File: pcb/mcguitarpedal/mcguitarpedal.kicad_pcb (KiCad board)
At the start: 2 copper layers, 123 x 118 mm, 98 parts, among them J1 IN, J10 ENCODER2, J11 ENCODER3, J2 PREAMP_HEADERS, J3 BTN_MTX, J4 OUT, J5 EXP, J6 ILI9488 Module, J7 PWR_IN, J8 POT_HP_VOLUME_10k, J9 ENCODER1, Q1 Q_NPN_BCE, Q2 Q_PNP_BCE, SW1 SW_BYPASS, SW2 SW_TUNER, SW3 SW_PRESET, SW4 LINE_LEVEL, SW5 SW_PWR, U1 Teensy4.1, U2 Teensy Audio Board, U3 LM4562, U4 74HC148, U6 STPDWN-3P-5V, U7 STDN-3A24-ADJ, U8 74HCT595D

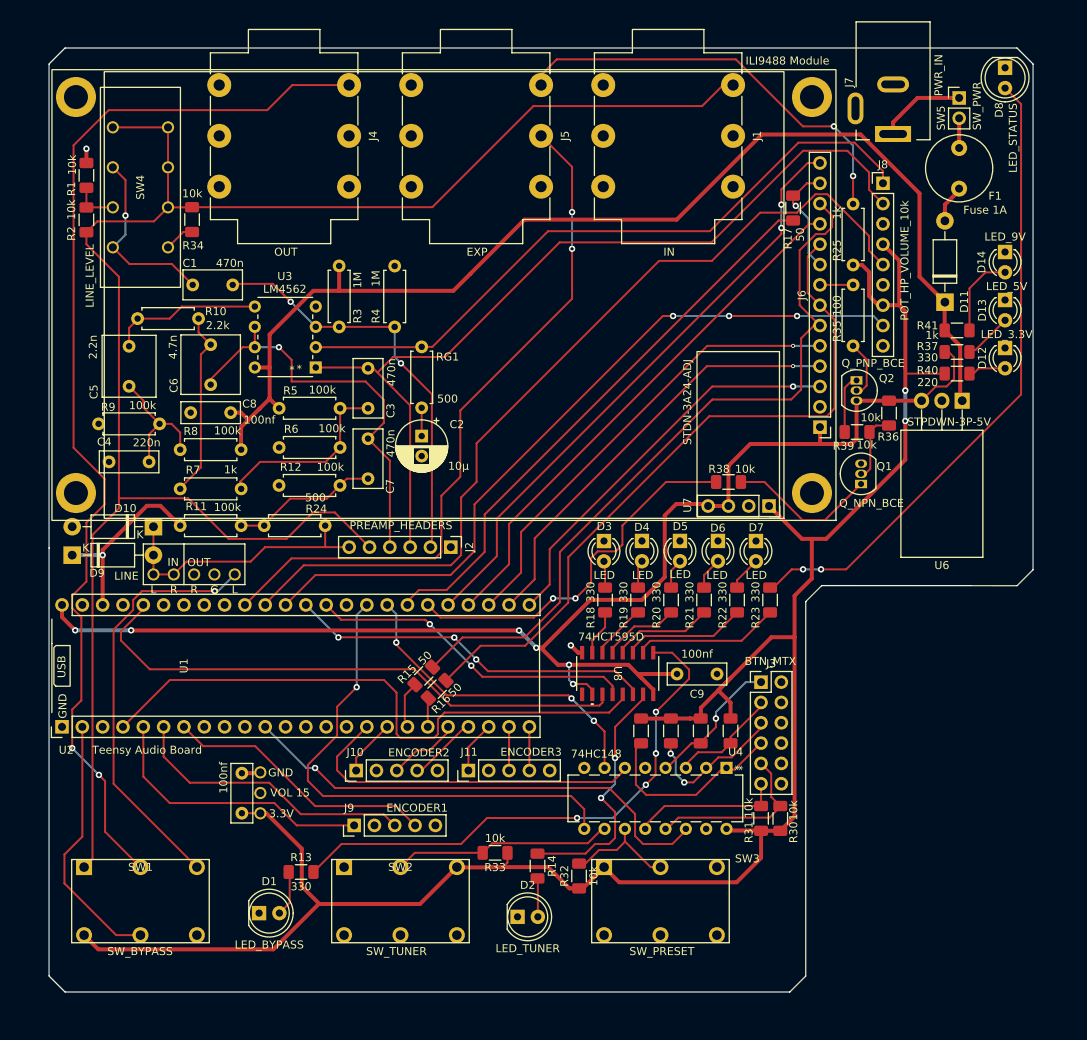
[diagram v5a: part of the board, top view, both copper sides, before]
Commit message: Rearranged pullups
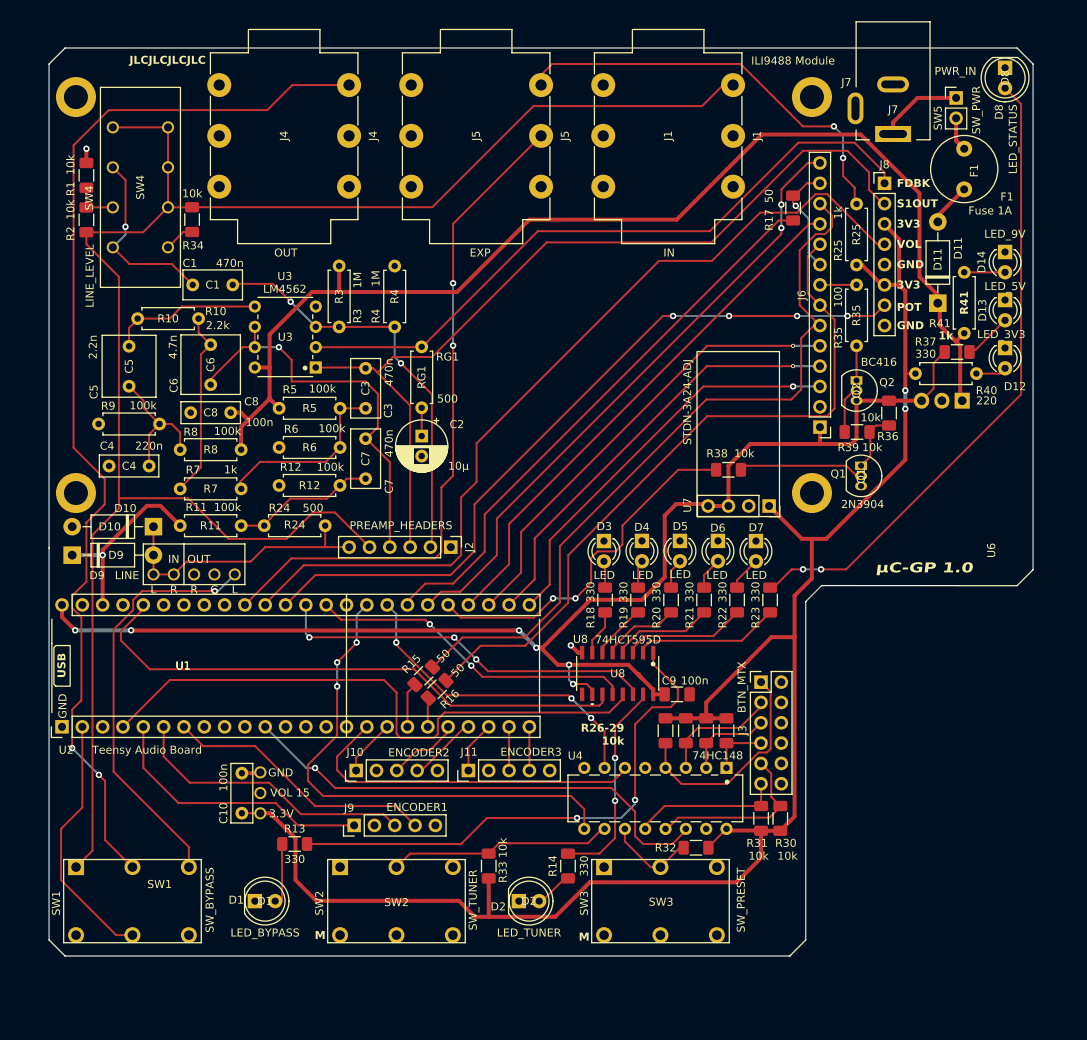
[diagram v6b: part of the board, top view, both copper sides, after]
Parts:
- C10, C8: value 100nf -> 100n
- C9: value 100nf -> 100n; footprint Capacitor_THT:C_Rect_L7.2mm_W2.5mm_P5.00mm_FKS2_FKP2_MKS2_MKP2 -> Capacitor_SMD:C_1206_3216Metric_Pad1.33x1.80mm_HandSolder
- D12: value LED_3.3V -> LED_3V3
- J8: footprint Connector_PinHeader_2.54mm:PinHeader_1x09_P2.54mm_Vertical -> mcguitarpedal:POTS_HEADER
- Q1: value Q_NPN_BCE -> 2N3904
- Q2: value Q_PNP_BCE -> BC416
- R40, R41: footprint Resistor_SMD:R_1206_3216Metric_Pad1.30x1.75mm_HandSolder -> Resistor_THT:R_Axial_DIN0207_L6.3mm_D2.5mm_P7.62mm_Horizontal
- U1: footprint mcguitarpedal:Teensy 4.1 -> mcguitarpedal:Teensy 4.1 with audio board
- U6: footprint Package_TO_SOT_THT:TO-220-3_Horizontal_TabDown -> mcguitarpedal:STPDWN-3P-5V
- moved R32 15.0 mm to (134.4, 125.0), turned to 180 degrees
- moved R26 10.7 mm to (138.2, 110.3)
- moved R41 7.31 mm to (167.9, 53.0), turned to -90 degrees
- moved C9 5.60 mm to (132.0, 105.8)
- moved R28 5.59 mm to (133.1, 110.3)
- moved R27 4.41 mm to (135.6, 110.3)
- moved R29 4.40 mm to (130.6, 110.3)
- moved R14 3.81 mm to (118.4, 127.3)
- moved R13 3.59 mm to (84.2, 124.5)
- moved R40 2.42 mm to (169.4, 65.7)
- moved Q1 2.28 mm to (155.0, 77.2), turned to -90 degrees
- moved D2 1.97 mm to (112.2, 131.6)
- moved R33 1.83 mm to (108.5, 127.3), turned to 90 degrees
- moved D1 1.59 mm to (79.2, 131.6)
- moved R38 1.53 mm to (138.4, 77.7)
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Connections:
- net /LED_STR renamed /22_LED_SHIFT_CLK
- net /SCK renamed /13_LED_STORE_CLK
- J6 pad 14: /37_TFT_T_IRQ -> /38_TFT_T_IRQ
- Q1 pad 1: Net-(Q1-B) -> Net-(Q1-C)
- Q1 pad 2: Net-(Q1-C) -> Net-(Q1-B)
- Q2 pad 1: Net-(Q2-B) -> Net-(Q2-C)
- Q2 pad 2: Net-(Q2-C) -> Net-(Q2-B)
- R38 pad 1: /38_BACKLIGHT_PWM -> /37_BACKLIGHT_PWM
- SW1 pad 4: 3.3V -> GND
- SW1 pad 6: GND -> unconnected-(SW1-C-Pad6)
- SW2 pad 3: 3.3V -> unconnected-(SW2-C-Pad3)
- SW3 pad 1: 3.3V -> GND
- SW3 pad 3: GND -> unconnected-(SW3-C-Pad3)
- U1 pad 29: /37_TFT_T_IRQ -> /37_BACKLIGHT_PWM
- U1 pad 30: /38_BACKLIGHT_PWM -> /38_TFT_T_IRQ
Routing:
- net /38_TFT_T_IRQ: track 0.00 -> 77.9 mm, vias 0 -> 2
- net /37_TFT_T_IRQ: track 75.4 -> 0.00 mm, vias 2 -> 0
- net /38_BACKLIGHT_PWM: track 46.9 -> 0.00 mm, vias 2 -> 0
- net /37_BACKLIGHT_PWM: track 0.00 -> 45.0 mm, vias 0 -> 2
- net 3.3V: track 260.1 -> 217.9 mm
- net Net-(J3-Pin_7): track 24.3 -> 7.42 mm
- net Net-(J3-Pin_1): track 17.3 -> 27.7 mm, vias 1 -> 0
- net Net-(J3-Pin_5): track 18.0 -> 11.0 mm, vias 2 -> 0
- net Net-(D14-A): track 10.5 -> 5.11 mm
- net Net-(U8-Q0): track 30.8 -> 25.6 mm
- net 5V: track 172.3 -> 167.4 mm
- net /A3_EXP: track 87.7 -> 84.5 mm
- net Net-(Q1-B): track 18.9 -> 15.8 mm
- net /SW3: track 14.1 -> 11.0 mm
- net Net-(Q2-C): track 7.20 -> 4.32 mm
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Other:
- board size 123 x 118 mm -> 123 x 113.5 mm
- board text added: "JLCJLCJLCJLC"
- board text added: "M"
- board text added: "R26-29 10k"
- board text added: "TODO: Testpoints Mounting holes Header silkscreen labels Silkscreen in general Decoupling caps for U4-7 (SMD ceramic?) Double check 8-to-3 pinout"
- board text added: "µC-GP 1.0"
- board text removed: "TODO: Backlight brightness PWR and status LEDs Testpoints Mounting holes Header silkscreen labels Silkscreen in general Decrease board size (Move inputs down?) Decoupling caps for U4-7 (SMD ceramic?)"

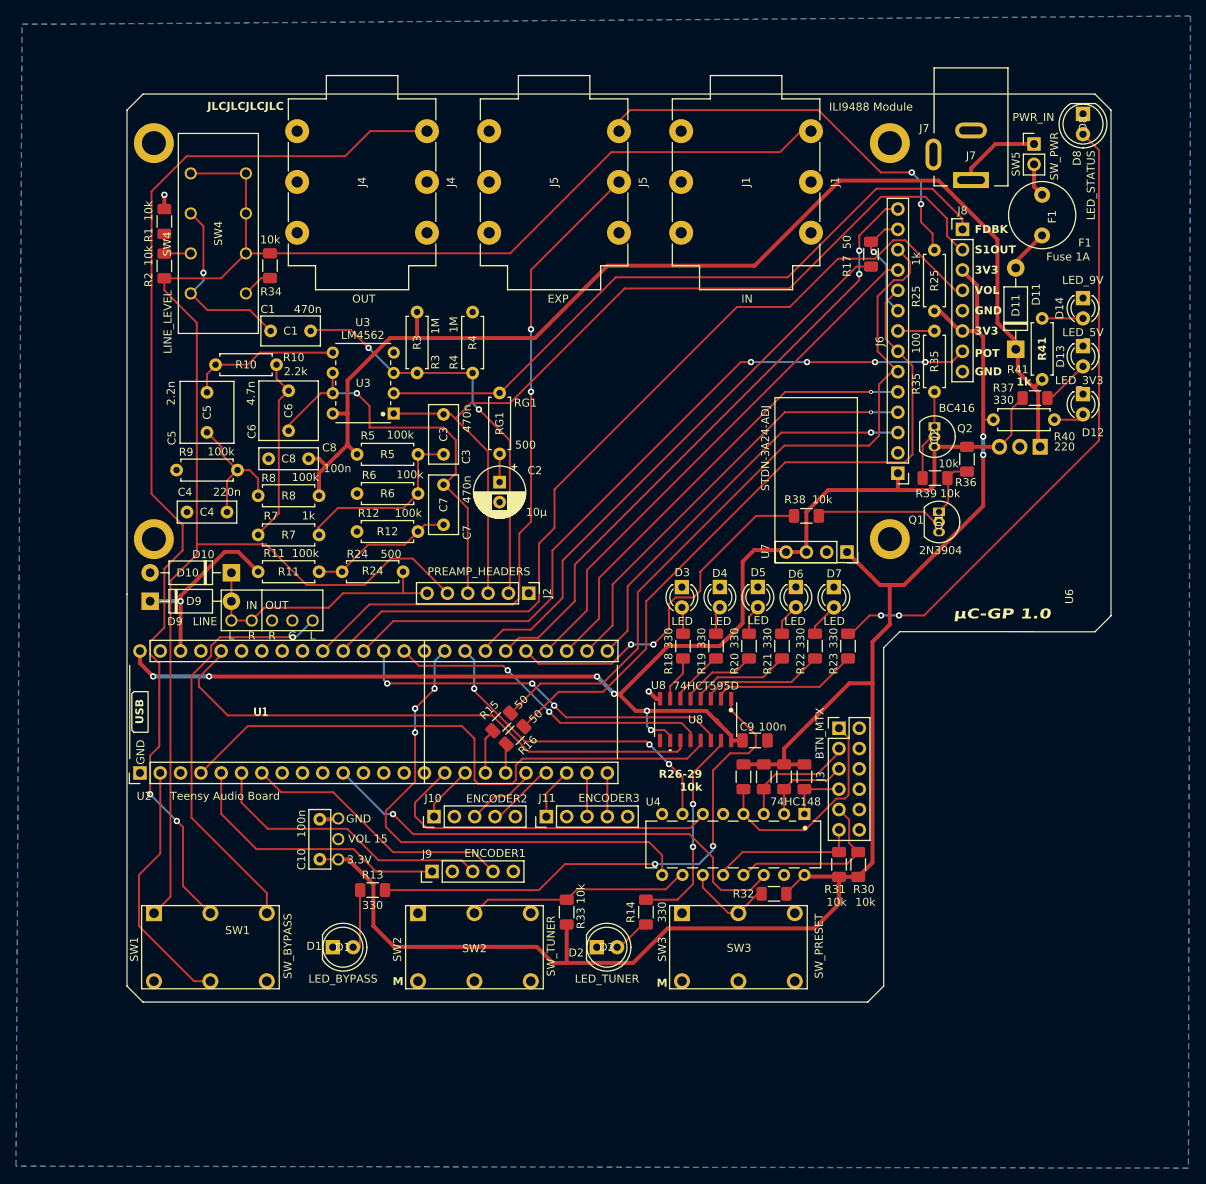
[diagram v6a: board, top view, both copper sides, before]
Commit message: Silkscreen labeling
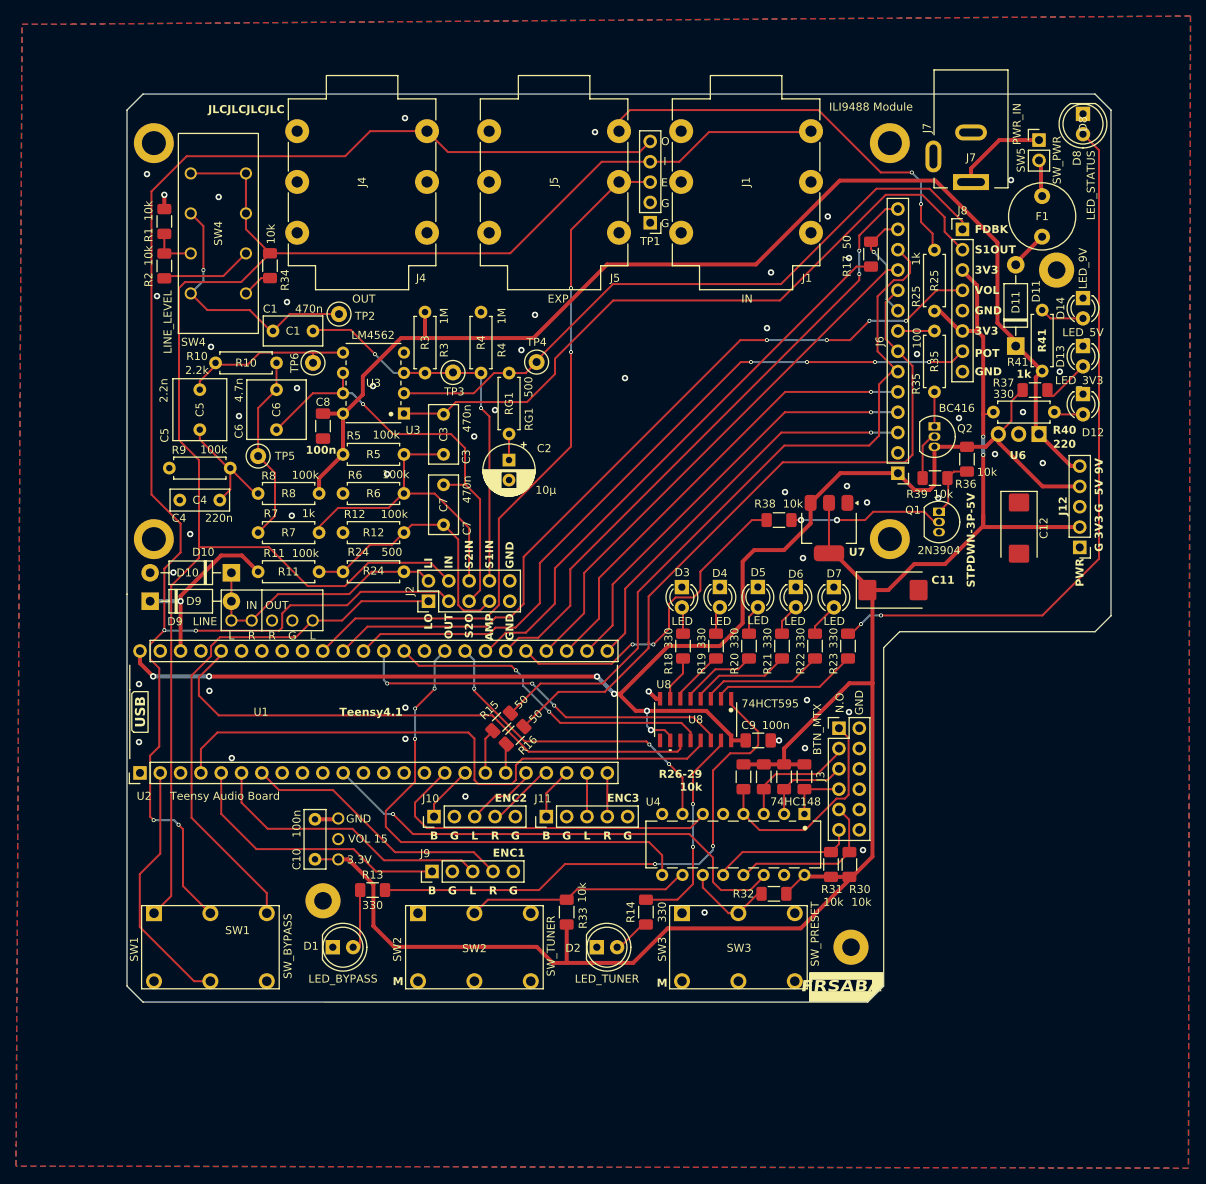
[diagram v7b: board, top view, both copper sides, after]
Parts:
- added C11: 22u, Capacitor_Tantalum_SMD:CP_EIA-7343-30_AVX-N_Pad2.25x2.55mm_HandSolder, F.Cu at (149.2, 87.0)
- added C12: 22u, Capacitor_Tantalum_SMD:CP_EIA-7343-30_AVX-N_Pad2.25x2.55mm_HandSolder, F.Cu at (165.0, 79.2)
- added H1: MountingHole_Pad, MountingHole:MountingHole_2.2mm_M2_Pad, F.Cu at (78.0, 125.8)
- added H2: MountingHole_Pad, MountingHole:MountingHole_2.2mm_M2_Pad, F.Cu at (144.0, 131.6)
- added H3: MountingHole_Pad, MountingHole:MountingHole_2.2mm_M2_Pad, F.Cu at (169.7, 47.0)
- added J12: PWR, Connector_PinHeader_2.54mm:PinHeader_1x05_P2.54mm_Vertical, F.Cu at (172.6, 81.7)
- added TP1: TP_SIGNAL, Connector_PinHeader_2.54mm:PinHeader_1x05_P2.54mm_Vertical, F.Cu at (118.9, 41.1)
- added TP2: TestPoint, TestPoint:TestPoint_Loop_D1.80mm_Drill1.0mm_Beaded, F.Cu at (80.0, 52.5)
- added TP3: TestPoint, TestPoint:TestPoint_Loop_D1.80mm_Drill1.0mm_Beaded, F.Cu at (94.2, 59.8)
- added TP4: TestPoint, TestPoint:TestPoint_Loop_D1.80mm_Drill1.0mm_Beaded, F.Cu at (104.7, 58.5)
- added TP5: TestPoint, TestPoint:TestPoint_Loop_D1.80mm_Drill1.0mm_Beaded, F.Cu at (69.9, 70.2)
- added TP6: TestPoint, TestPoint:TestPoint_Loop_D1.80mm_Drill1.0mm_Beaded, F.Cu at (76.8, 58.6)
- C8: footprint Capacitor_THT:C_Rect_L7.2mm_W2.5mm_P5.00mm_FKS2_FKP2_MKS2_MKP2 -> Capacitor_SMD:C_1206_3216Metric_Pad1.33x1.80mm_HandSolder
- J10: value ENCODER2 -> ENC2; footprint Connector_PinHeader_2.54mm:PinHeader_1x05_P2.54mm_Vertical -> mcguitarpedal:Encoder_headers
- J11: value ENCODER3 -> ENC3; footprint Connector_PinHeader_2.54mm:PinHeader_1x05_P2.54mm_Vertical -> mcguitarpedal:Encoder_headers
- J2: footprint Connector_PinHeader_2.54mm:PinHeader_1x06_P2.54mm_Vertical -> mcguitarpedal:PREAMP_HEADERS
- J9: value ENCODER1 -> ENC1; footprint Connector_PinHeader_2.54mm:PinHeader_1x05_P2.54mm_Vertical -> mcguitarpedal:Encoder_headers
- U7: value STDN-3A24-ADJ -> AMS1117-3.3; footprint mcguitarpedal:STPDN-3A24-ADJ -> Package_TO_SOT_SMD:SOT-223-3_TabPin2
- U8: value 74HCT595D -> 74HCT595
- moved J2 12.6 mm to (91.2, 88.4), turned to 90 degrees
- moved C8 4.46 mm to (78.0, 66.5), turned to -90 degrees
- moved U7 3.75 mm to (141.2, 79.2)
- moved R38 3.47 mm to (135.0, 78.2)
- moved C2 3.00 mm to (101.2, 70.8)
- moved RG1 2.75 mm to (101.3, 59.9)
- moved R6 1.76 mm to (88.1, 74.9)
- moved R5 1.76 mm to (80.5, 70.0)
- moved R12 1.75 mm to (88.1, 79.8)
- moved C4 1.75 mm to (65.1, 75.8)
- moved U6 1.59 mm to (167.5, 67.5)
- moved C6 1.52 mm to (72.2, 67.0)
- moved U3 1.28 mm to (88.1, 64.9)
- moved R30 1.10 mm to (143.8, 121.3)
- moved R4 1.05 mm to (97.8, 59.9)
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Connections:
- J2 pad 1: GND -> /LINE_OUT
- J2 pad 2: /preamp/STAGE1_IN -> /LINE_IN
- J2 pad 3: /preamp/STAGE1_OUT -> /SIGNAL_OUT
- J2 pad 4: /preamp/STAGE2_OUT -> /SIGNAL_IN
- J2 pad 5: /SIGNAL_IN -> /preamp/STAGE2_OUT
- J2 pad 6: /LINE_IN -> /preamp/STAGE2_IN
- R2 pad 2: /SIGNAL_IN -> Net-(R2-Pad2)
- SW4 pad 6: /SIGNAL_IN -> Net-(R2-Pad2)
- U7 pad 1: 3.3V -> GND
- U7 pad 2: GND -> 3.3V
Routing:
- net /SIGNAL_OUT: track 134.6 -> 204.5 mm, vias 2 -> 4
- net /preamp/STAGE1_OUT: track 110.2 -> 86.4 mm
- net 3.3V: track 217.9 -> 239.7 mm
- net /preamp/STAGE2_IN: track 23.5 -> 39.2 mm
- net /LINE_OUT: track 52.3 -> 67.8 mm, vias 1 -> 0
- net /preamp/PREAMP_OUT: track 18.3 -> 33.8 mm
- net 5V: track 167.4 -> 178.6 mm
- net Net-(R2-Pad2): track 0.00 -> 11.1 mm
- net Net-(SW4-D): track 23.2 -> 32.4 mm
- net /A2_VOLUME: track 108.3 -> 99.5 mm, vias 0 -> 4
- net Net-(D8-A): track 80.1 -> 88.7 mm
- net /SIGNAL_IN: track 224.5 -> 220.7 mm
- net /37_BACKLIGHT_PWM: track 45.0 -> 41.4 mm
- net /preamp/STAGE2_OUT: track 50.7 -> 54.0 mm
- net Net-(Q1-B): track 15.8 -> 18.8 mm, vias 0 -> 2
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- added copper zone on F.Cu, net GND
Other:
- rule pad_to_mask_clearance: 0 -> 0.038
- board text added: "3V3"
- board text added: "5V"
- board text added: "9V"
- board text added: "E"
- board text added: "FRSABA"
- board text added: "G"
- board text added: "GND"
- board text added: "I"
- board text added: "N.O"
- board text added: "O"
- board text added: "TODO: Display testpoints? Mounting holes Decoupling caps for U4-7 (SMD ceramic?)"
- board text removed: "TODO: Testpoints Mounting holes Header silkscreen labels Silkscreen in general Decoupling caps for U4-7 (SMD ceramic?) Double check 8-to-3 pinout"
- board text removed: "µC-GP 1.0"

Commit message: Final 1.0 design
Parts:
- added C1: 22u, Capacitor_Tantalum_SMD:CP_EIA-3216-18_Kemet-A_Pad1.58x1.35mm_HandSolder, F.Cu at (137.5, 73.5)
- added C2: 100n, Capacitor_SMD:C_1206_3216Metric_Pad1.33x1.80mm_HandSolder, F.Cu at (135.1, 76.0)
- added C4: 100n, Capacitor_SMD:C_1206_3216Metric_Pad1.33x1.80mm_HandSolder, F.Cu at (167.5, 68.2)
- added C6: 22u, Capacitor_Tantalum_SMD:CP_EIA-3216-18_Kemet-A_Pad1.58x1.35mm_HandSolder, F.Cu at (72.4, 120.7)
- added C9: 100n, Capacitor_SMD:C_1206_3216Metric_Pad1.33x1.80mm_HandSolder, F.Cu at (139.7, 125.0)
- added H1: MountingHole_Pad, MountingHole:MountingHole_2.2mm_M2_Pad, F.Cu at (94.9, 49.0)
- added R20: 10k, Resistor_SMD:R_1206_3216Metric_Pad1.30x1.75mm_HandSolder, F.Cu at (154.4, 48.1)
- added TP2: SHIFT_CLK, TestPoint:TestPoint_Loop_D1.80mm_Drill1.0mm_Beaded, F.Cu at (117.5, 109.8)
- added TP3: TP_LED_DATA, TestPoint:TestPoint_Loop_D1.80mm_Drill1.0mm_Beaded, F.Cu at (117.5, 99.8)
- added TP4: TP_STORE_CLK, TestPoint:TestPoint_Loop_D1.80mm_Drill1.0mm_Beaded, F.Cu at (117.5, 103.9)
- added TP5: TP_MOSI, TestPoint:TestPoint_Loop_D1.80mm_Drill1.0mm_Beaded, F.Cu at (142.5, 68.8)
- added TP6: TP_SCLK, TestPoint:TestPoint_Loop_D1.80mm_Drill1.0mm_Beaded, F.Cu at (146.2, 70.5)
- added TP7: TP_MISO, TestPoint:TestPoint_Loop_D1.80mm_Drill1.0mm_Beaded, F.Cu at (138.2, 51.8)
- C3: renamed from C11; footprint Capacitor_Tantalum_SMD:CP_EIA-7343-30_AVX-N_Pad2.25x2.55mm_HandSolder -> Capacitor_Tantalum_SMD:CP_EIA-3216-18_Kemet-A_Pad1.58x1.35mm_HandSolder
- C5: renamed from C12; footprint Capacitor_Tantalum_SMD:CP_EIA-7343-30_AVX-N_Pad2.25x2.55mm_HandSolder -> Capacitor_Tantalum_SMD:CP_EIA-3216-18_Kemet-A_Pad1.58x1.35mm_HandSolder
- R16: renamed from R25; value 1k -> 330; footprint Resistor_THT:R_Axial_DIN0207_L6.3mm_D2.5mm_P7.62mm_Horizontal -> Resistor_SMD:R_1206_3216Metric_Pad1.30x1.75mm_HandSolder
- U3: footprint LM4562:lm4562 -> TI_FOOTPRINTS:lm4562
- moved C5 9.57 mm to (163.9, 69.8), turned to 0 degrees
- moved R3 5.75 mm to (169.2, 46.4)
- moved U4 5.25 mm to (167.5, 72.8)
- moved H3 4.31 mm to (172.8, 44.0)
- moved R16 2.59 mm to (154.4, 41.9)
- moved R4 2.40 mm to (166.9, 59.6)
- moved C3 2.37 mm to (147.0, 86.2)
- moved R14 1.89 mm to (158.5, 68.8)
- moved R5 1.75 mm to (169.4, 63.0)
- moved F1 1.26 mm to (168.1, 36.5)
- moved R13 1.23 mm to (133.8, 78.5)
- moved R21 0.91 mm to (133.5, 125.2)
- moved SW1 0.75 mm to (167.5, 30.0)
- moved SW2 0.61 mm to (56.9, 128.0)
- moved SW3 0.61 mm to (89.9, 128.0)
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- renumbered C1 to C10, C2 to C11, C3 to C12, C4 to C13, C5 to C14, C6 to C15, C7 to C16, C8 to C17, C10 to C7, C9 to C8, D11 to D1, D7 to D10, D6 to D11, D5 to D12, D4 to D13, D3 to D14, D9 to D2, D10 to D3, D2 to D4, D14 to D5, D13 to D6, D12 to D7, D1 to D8, D8 to D9, H1 to H2, H2 to H4, J4 to J1, J3 to J12, J5 to J2, J1 to J3, J12 to J4, J7 to J5, J2 to J6, J6 to J7, R24 to R1, R20 to R10, R19 to R11, R18 to R12, R38 to R13, R36 to R14, R39 to R15, R35 to R17, R33 to R18, R26 to R19, R14 to R2, R32 to R21, R27 to R22, R28 to R23, R31 to R24, R29 to R25, R30 to R26, R15 to R27, R16 to R28, R17 to R29, R41 to R3, R34 to R30, R2 to R31, R1 to R32, R3 to R33, R4 to R34, R5 to R35, R6 to R36, R7 to R37, R8 to R38, R9 to R39, R37 to R4, R10 to R40, R11 to R41, R12 to R42, R40 to R5, R13 to R6, R23 to R7, R22 to R8, R21 to R9, SW5 to SW1, SW1 to SW2, SW2 to SW3, SW3 to SW4, SW4 to SW5, TP4 to TP10, TP5 to TP11, TP6 to TP12, TP2 to TP8, TP3 to TP9, U6 to U4, U7 to U5, U8 to U6, U4 to U7
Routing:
- net 3.3V: track 239.7 -> 251.5 mm
- net 9V: track 148.7 -> 159.6 mm
- net 5V: track 178.6 -> 189.1 mm, vias 6 -> 4
- net /36_TOUCH_CS: track 66.6 -> 71.7 mm, vias 0 -> 1
- net Net-(J2-PadT): track 52.4 -> 47.7 mm
- net /41_BTN_MTX_A: track 63.7 -> 59.5 mm
- net /22_LED_SHIFT_CLK: track 70.5 -> 73.3 mm, vias 0 -> 1
- net Net-(D5-A): track 5.54 -> 8.21 mm
- net /14_LED_DATA: track 47.4 -> 49.5 mm, vias 3 -> 5
- net Net-(D1-A): track 4.66 -> 6.60 mm
- net GND: track 7.42 -> 9.31 mm, vias 50 -> 83
- net Net-(Q1-C): track 7.37 -> 9.08 mm
- net Net-(D9-A): track 88.7 -> 90.1 mm
- net /2_LED_PWM: track 75.1 -> 73.7 mm
- net /13_LED_STORE_CLK: track 41.6 -> 40.3 mm, vias 2 -> 3
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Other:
- board text added: "DS"
- board text added: "SH_CP"
- board text added: "ST_CP"
- board text added: "U3"
- board text removed: "TODO: Display testpoints? Mounting holes Decoupling caps for U4-7 (SMD ceramic?)"
